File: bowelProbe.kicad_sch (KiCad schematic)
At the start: 8 parts, among them J1 Probe, U2 AD8001AN, U3 AD8001AN

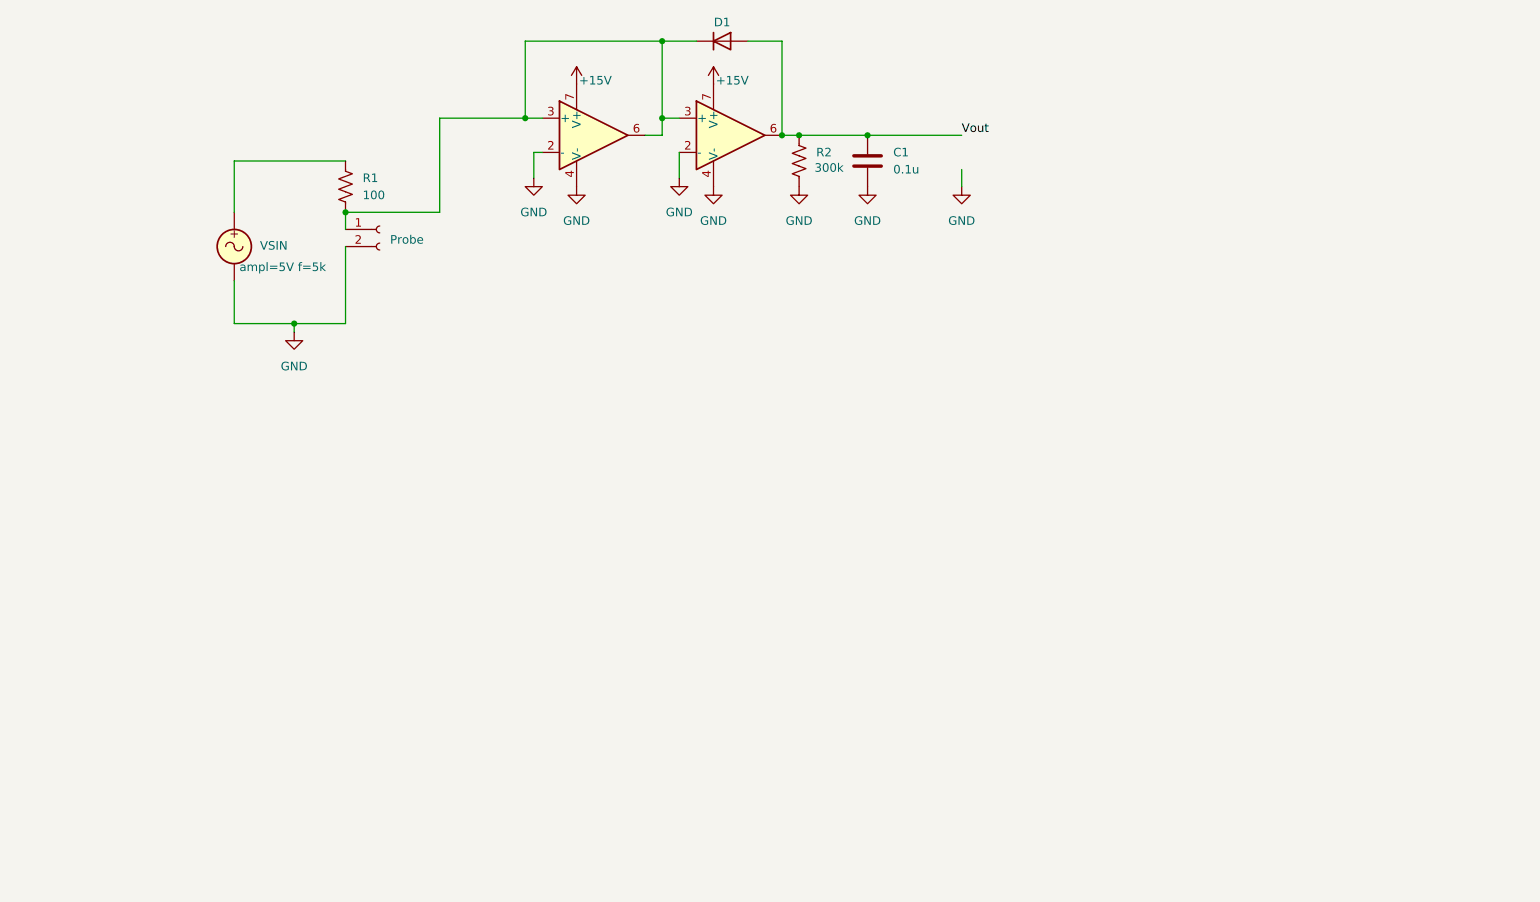
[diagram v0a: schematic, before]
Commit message: Finished Schematic
Schematic was updated and completed. Awaiting final checks to ensure proper wiring.

Next steps: choose components, assign footprints accordingly, begin PCB placement and routing.
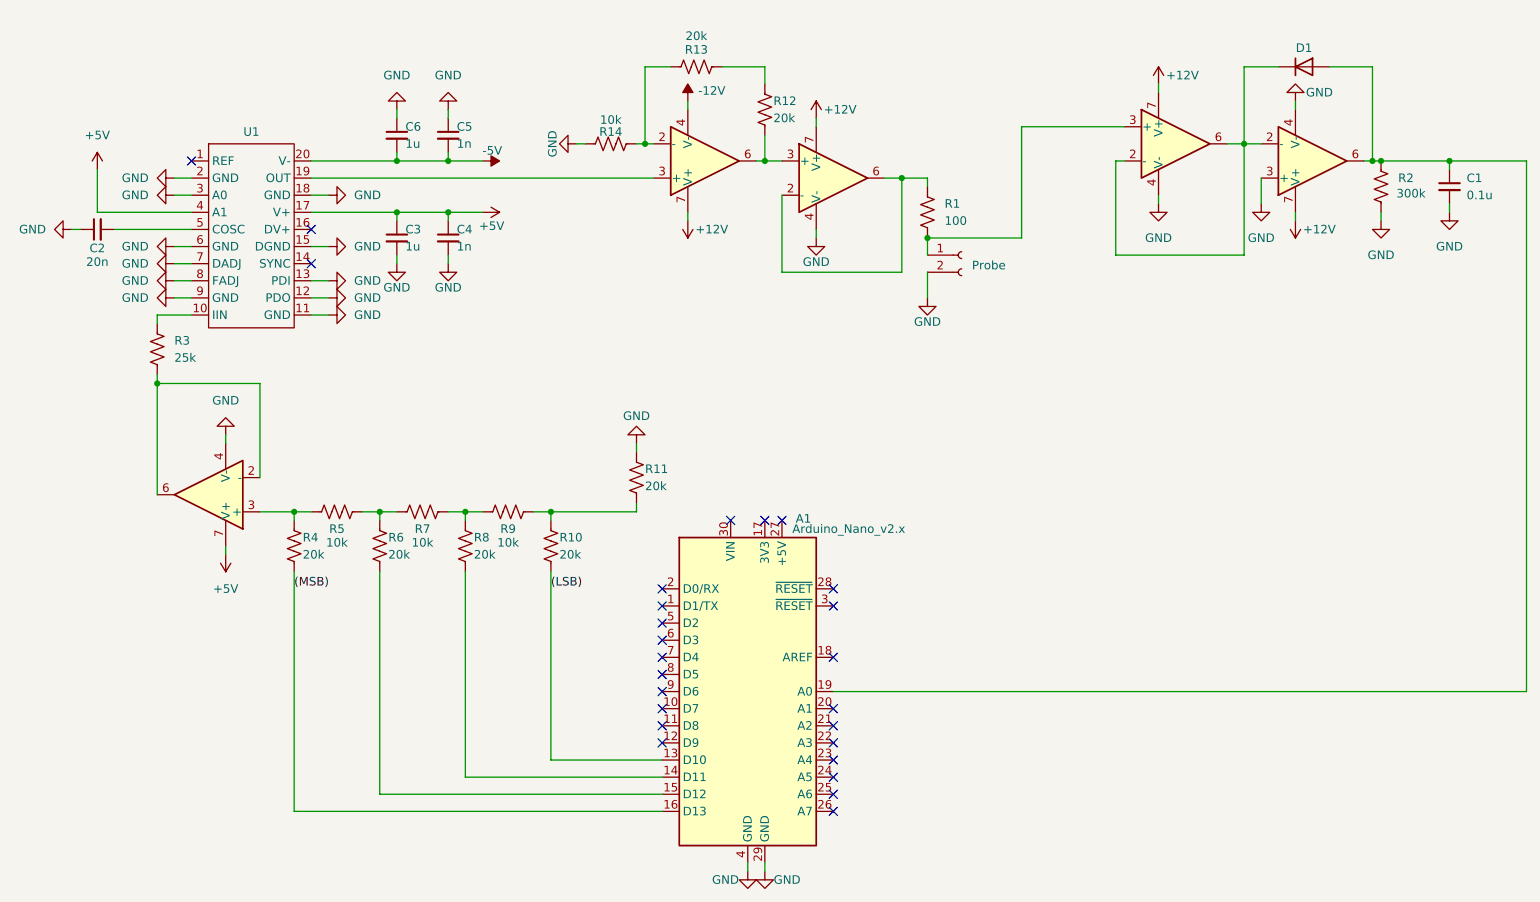
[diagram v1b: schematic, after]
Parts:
- removed C1: 0.1u, symbol Device:C
- removed V1: VSIN, symbol Simulation_SPICE:VSIN
- added A1: Arduino_Nano_v2.x, Module:Arduino_Nano, symbol MCU_Module:Arduino_Nano_v2.x
- added C1: 0.1u, symbol Device:C_Small
- added C2: 20n, symbol Device:C_Small
- added C3, C6: 1u, symbol Device:C_Small
- added C4, C5: 1n, symbol Device:C_Small
- added R10, R11, R12, R13, R4, R6, R8: 20k, symbol Device:R_US
- added R14, R5, R7, R9: 10k, symbol Device:R_US
- added R3: 25k, symbol Device:R_US
- added U1: ~, symbol BowelProbe:MAX038CPP
- added U4: (no value), symbol Amplifier_Operational:AD8001AN
- added U5, U6: ~, symbol Amplifier_Operational:AD8001AN
- D1: value 1N4001 -> ~; footprint Diode_THT:D_DO-41_SOD81_P10.16mm_Horizontal -> (none)
- U2, U3: value AD8001AN -> ~; footprint Package_DIP:DIP-8_W7.62mm -> (none)
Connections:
- net GND: now also U2.3 (+), A1.29 (GND), A1.4 (GND), C1.2, C2.1, C3.2, C4.2, C5.1, C6.1, R11.1, R14.1, U1.11 (GND), U1.12 (PDO), U1.13 (PDI), U1.15 (DGND), U1.18 (GND), U1.2 (GND), U1.3 (A0), U1.6 (GND), U1.7 (DADJ), U1.8 (FADJ), U1.9 (GND), U4.4 (V-), U6.4 (V-); no longer U2.2 (-), U3.2 (-)
- net at J1.1 (Pin_1), R1.2, U3.3 (+): no longer D1.1 (K), U2.3 (+), U3.6
- net at R1.1: now also U6.2 (-), U6.6
- net +15V renamed +12V
- net +12V: now also U5.7 (V+), U6.7 (V+)
- net Vout: no longer names the net of D1.2 (A), R2.1, U2.6
- net Vout: now also A1.19 (A0), C1.1
- new net: R4.1, R5.1, U4.3 (+)
- new net: D1.1 (K), U2.2 (-), U3.2 (-), U3.6
- new net: R10.1, R11.2, R9.2
- new net: R5.2, R6.1, R7.1
- new net: R7.2, R8.1, R9.1
- new net: R12.1, R13.1
- new net: R13.2, R14.2, U5.2 (-)
- new net: U1.19 (OUT), U5.3 (+)
- new net: R12.2, U5.6, U6.3 (+)
- new net: R3.1, U1.10 (IIN)
- new net: R3.2, U4.2 (-), U4.6
- new net: A1.14 (D11), R8.2
- new net: C2.2, U1.5 (COSC)
- new net: A1.15 (D12), R6.2
- new net (LSB): A1.13 (D10), R10.2
- new net (MSB): A1.16 (D13), R4.2
- new net +5V: C3.1, C4.1, U1.17 (V+), U1.4 (A1), U4.7 (V+)
- new net -12V: U5.4 (V-)
- new net -5V: C5.2, C6.2, U1.20 (V-)
- no-connect marks 0 -> 26
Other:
- moved on the sheet: D1, R1, R2
